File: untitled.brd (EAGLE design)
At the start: 95 x 55 mm, 26 parts, among them IC1 L297, IC2 L298

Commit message: Another commit
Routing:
- net N$9: track 59.8 -> 55.4 mm, vias 0 -> 2
- net N$19: track 80.8 -> 79.5 mm
- net N$8: track 37.3 -> 36.4 mm
- net +24V: track 190.9 -> 190.2 mm, vias 2 -> 0
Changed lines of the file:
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@@
 <wire x1="26" y1="8.035" x2="26" y2="6" width="1.9304" layer="16"/>
 <wire x1="26" y1="6" x2="28" y2="4" width="1.9304" layer="16"/>
-<wire x1="28" y1="4" x2="36" y2="4" width="1.9304" layer="16"/>
-<wire x1="36" y1="4" x2="82" y2="4" width="1.9304" layer="16"/>
+<wire x1="28" y1="4" x2="38" y2="4" width="1.9304" layer="16"/>
+<wire x1="38" y1="4" x2="82" y2="4" width="1.9304" layer="16"/>
 <wire x1="82" y1="4" x2="92" y2="14" width="1.9304" layer="16"/>
 <wire x1="92" y1="14" x2="92" y2="40" width="1.9304" layer="16"/>
@@
 <wire x1="18.73" y1="16.46" x2="18.75" y2="17.98" width="1.9304" layer="16"/>
 <wire x1="65" y1="46.62" x2="65" y2="50.73" width="1.9304" layer="16"/>
-<wire x1="41.54" y1="27.92" x2="38.92" y2="27.92" width="1.778" layer="16"/>
-<wire x1="38.92" y1="27.92" x2="36" y2="25" width="1.778" layer="16"/>
-<wire x1="36" y1="25" x2="36" y2="14" width="1.778" layer="16"/>
-<wire x1="36" y1="4" x2="36" y2="9" width="1.778" layer="16"/>
-<via x="36" y="9" extent="1-16" drill="1" shape="square"/>
-<via x="36" y="14" extent="1-16" drill="1" shape="square"/>
-<wire x1="36" y1="9" x2="36" y2="14" width="0.8128" layer="1"/>
+<wire x1="41.54" y1="27.92" x2="41.54" y2="28" width="1.778" layer="16"/>
+<wire x1="41.54" y1="28" x2="39" y2="28" width="1.778" layer="16"/>
+<wire x1="39" y1="28" x2="38" y2="27" width="1.778" layer="16"/>
+<wire x1="38" y1="27" x2="38" y2="4" width="1.778" layer="16"/>
 </signal>
 <signal name="N$5">
@@
 <wire x1="32.81" y1="31.73" x2="31.73" y2="31.73" width="0.3048" layer="16"/>
 <wire x1="31.73" y1="31.73" x2="30.5" y2="30.5" width="0.3048" layer="16"/>
-<wire x1="30.5" y1="30.5" x2="30.5" y2="16.295" width="0.3048" layer="16"/>
-<wire x1="30.5" y1="16.295" x2="29.07" y2="15.5" width="0.3048" layer="16"/>
+<wire x1="30.5" y1="30.5" x2="30.5" y2="17.295" width="0.3048" layer="16"/>
+<wire x1="30.5" y1="17.295" x2="29.07" y2="15.5" width="0.3048" layer="16"/>
 <wire x1="32.81" y1="31.73" x2="33.27" y2="31.73" width="0.3048" layer="16"/>
 <wire x1="33.27" y1="31.73" x2="34.54" y2="30.46" width="0.3048" layer="16"/>
@@
 <wire x1="25.84" y1="40" x2="27" y2="40" width="0.3048" layer="16"/>
 <wire x1="46.62" y1="41.89" x2="46" y2="42.51" width="0.3048" layer="16"/>
-<wire x1="46" y1="42.51" x2="46" y2="48.5" width="0.3048" layer="16"/>
-<via x="27" y="48.5" extent="1-16" drill="1" shape="square"/>
-<via x="46" y="48.5" extent="1-16" drill="1" shape="square"/>
-<wire x1="27" y1="48.5" x2="46" y2="48.5" width="0.3048" layer="1"/>
-<wire x1="27" y1="48.5" x2="28" y2="47.5" width="0.3048" layer="16"/>
+<wire x1="46" y1="42.51" x2="46" y2="48.25" width="0.3048" layer="16"/>
+<via x="27.25" y="48.25" extent="1-16" drill="1" shape="square"/>
+<via x="46" y="48.25" extent="1-16" drill="1" shape="square"/>
+<wire x1="27.25" y1="48.25" x2="46" y2="48.25" width="0.3048" layer="1"/>
+<wire x1="27.25" y1="48.25" x2="28" y2="47.5" width="0.3048" layer="16"/>
 <wire x1="28" y1="47.5" x2="28" y2="41" width="0.3048" layer="16"/>
 <wire x1="28" y1="41" x2="27" y2="40" width="0.3048" layer="16"/>
@@
 <contactref element="IC1" pad="14"/>
 <contactref element="IC2" pad="1"/>
-<wire x1="25.19" y1="36.81" x2="29" y2="33" width="0.3048" layer="16"/>
-<wire x1="27" y1="13.25" x2="28" y2="12.25" width="0.3048" layer="16"/>
-<wire x1="28" y1="12.25" x2="37" y2="12.25" width="0.3048" layer="16"/>
-<wire x1="37" y1="12.25" x2="38" y2="13.25" width="0.3048" layer="16"/>
-<wire x1="38" y1="13.25" x2="38" y2="25" width="0.3048" layer="16"/>
-<wire x1="38" y1="25" x2="39.75" y2="26.65" width="0.3048" layer="16"/>
-<wire x1="39.75" y1="26.65" x2="43.5" y2="26.65" width="0.3048" layer="16"/>
-<wire x1="43.5" y1="26.65" x2="46.14" y2="24.11" width="0.3048" layer="16"/>
-<wire x1="46.14" y1="24.11" x2="46.62" y2="24.11" width="0.3048" layer="16"/>
-<wire x1="29" y1="33" x2="29" y2="22" width="0.3048" layer="16"/>
-<wire x1="29" y1="22" x2="27" y2="20" width="0.3048" layer="16"/>
-<wire x1="27" y1="20" x2="27" y2="13.25" width="0.3048" layer="16"/>
+<wire x1="25.19" y1="36.81" x2="26.19" y2="36.81" width="0.3048" layer="16"/>
+<wire x1="26.19" y1="36.81" x2="29" y2="34" width="0.3048" layer="16"/>
+<wire x1="29" y1="34" x2="29" y2="21" width="0.3048" layer="16"/>
+<wire x1="29" y1="21" x2="27" y2="19" width="0.3048" layer="16"/>
+<wire x1="27" y1="19" x2="27" y2="14" width="0.3048" layer="16"/>
+<wire x1="27" y1="14" x2="28" y2="13" width="0.3048" layer="16"/>
+<wire x1="28" y1="13" x2="34" y2="13" width="0.3048" layer="16"/>
+<wire x1="34" y1="13" x2="36" y2="15" width="0.3048" layer="16"/>
+<wire x1="36" y1="15" x2="36" y2="22" width="0.3048" layer="16"/>
+<wire x1="46.62" y1="24.11" x2="46.62" y2="22.62" width="0.3048" layer="16"/>
+<wire x1="46.62" y1="22.62" x2="46" y2="22" width="0.3048" layer="16"/>
+<via x="36" y="22" extent="1-16" drill="0.6" shape="square"/>
+<via x="46" y="22" extent="1-16" drill="0.6" shape="square"/>
+<wire x1="36" y1="22" x2="46" y2="22" width="0.3048" layer="1"/>
 </signal>
 <signal name="N$7">
@@
 <wire x1="85" y1="41" x2="72" y2="41" width="1.9304" layer="16"/>
 <wire x1="65" y1="31.38" x2="65" y2="34" width="1.9304" layer="16"/>
-<wire x1="65" y1="34" x2="57" y2="42" width="1.9304" layer="16"/>
-<wire x1="57" y1="42" x2="52" y2="42" width="1.9304" layer="16"/>
-<wire x1="52" y1="42" x2="51" y2="43" width="1.9304" layer="16"/>
-<wire x1="51" y1="43" x2="51" y2="48.25" width="1.9304" layer="16"/>
-<wire x1="51" y1="48.25" x2="49" y2="50.25" width="1.9304" layer="16"/>
-<wire x1="49" y1="50.25" x2="44" y2="50.25" width="1.9304" layer="16"/>
-<wire x1="44" y1="50.25" x2="41.54" y2="47.79" width="1.9304" layer="16"/>
+<wire x1="48.75" y1="51.25" x2="44" y2="51.25" width="1.9304" layer="16"/>
+<wire x1="44" y1="51.25" x2="41.54" y2="47.79" width="1.9304" layer="16"/>
 <wire x1="41.54" y1="47.79" x2="41.54" y2="40.62" width="1.9304" layer="16"/>
 <wire x1="72" y1="41" x2="65" y2="34" width="1.9304" layer="16"/>
+<wire x1="64" y1="34" x2="65" y2="34" width="1.9304" layer="16"/>
+<wire x1="48.75" y1="51.25" x2="64" y2="34" width="1.9304" layer="16"/>
 </signal>
 <signal name="N$20">

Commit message: All traces routed
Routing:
- net N$19: track 79.5 -> 80.6 mm
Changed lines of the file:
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@@
 <wire x1="72" y1="41" x2="65" y2="34" width="1.9304" layer="16"/>
 <wire x1="64" y1="34" x2="65" y2="34" width="1.9304" layer="16"/>
-<wire x1="48.75" y1="51.25" x2="64" y2="34" width="1.9304" layer="16"/>
+<wire x1="48.75" y1="51.25" x2="51" y2="49" width="1.9304" layer="16"/>
+<wire x1="51" y1="49" x2="51" y2="46" width="1.9304" layer="16"/>
+<wire x1="51" y1="46" x2="63" y2="34" width="1.9304" layer="16"/>
+<wire x1="63" y1="34" x2="64" y2="34" width="1.9304" layer="16"/>
 </signal>
 <signal name="N$20">

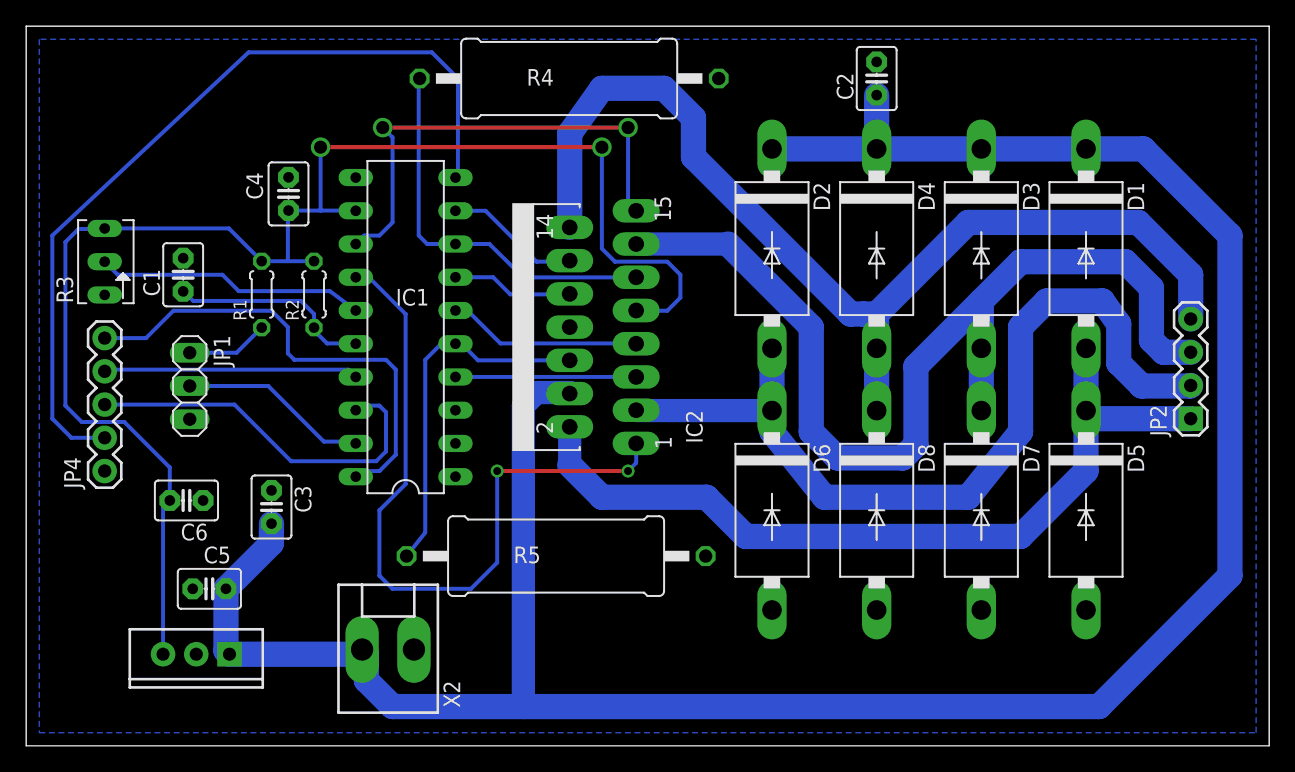
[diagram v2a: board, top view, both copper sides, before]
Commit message: Improved space between traces
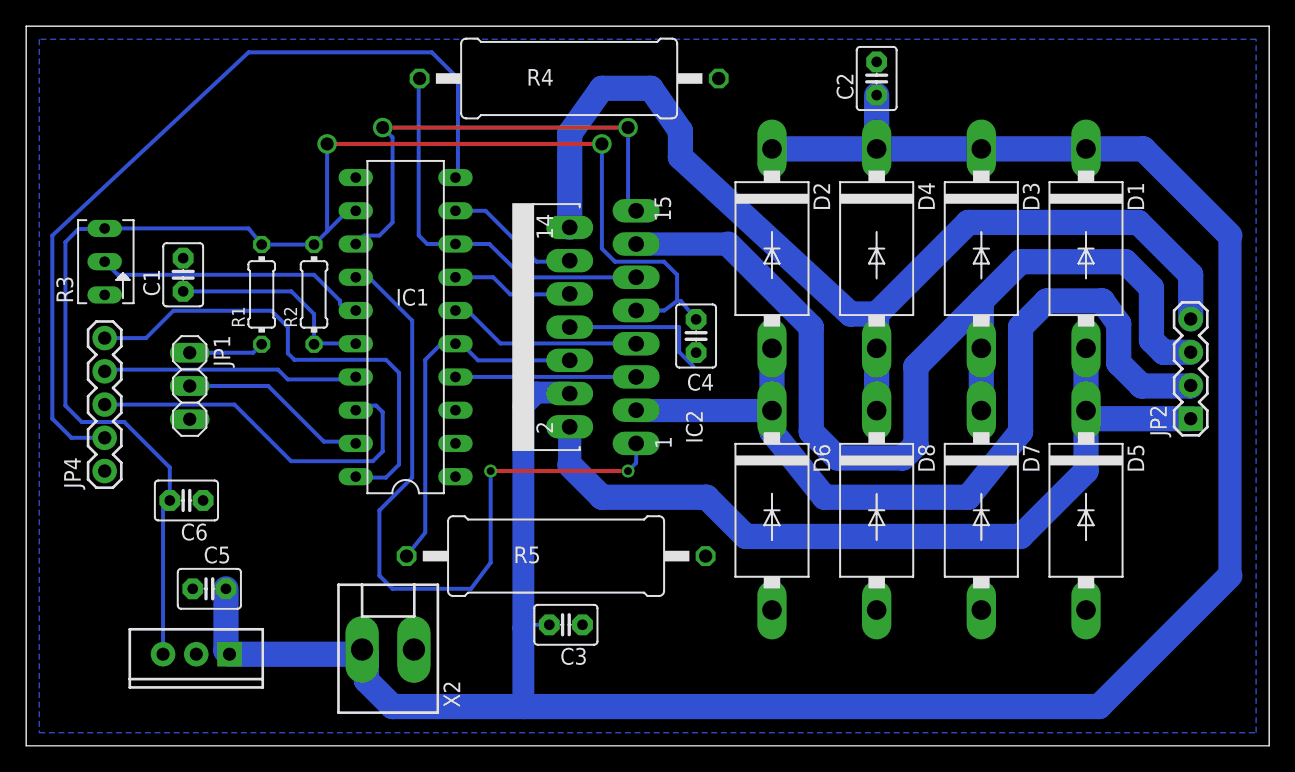
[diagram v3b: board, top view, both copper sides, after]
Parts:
- R1, R2: device resistor:0204/5 -> resistor:0204/7
- moved C4 33.0 mm to (51.2, 32.3), turned to 90 degrees
- moved C3 24.2 mm to (41.2, 10.2), turned to 180 degrees
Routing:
- net GND: track 0.00 -> 11.8 mm
- net +24V: track 190.2 -> 185.8 mm
- net +5V: track 113.7 -> 111.0 mm
- net N$13: track 36.6 -> 37.5 mm
- net N$20: track 15.6 -> 16.2 mm
- net N$9: track 55.4 -> 56.0 mm
- net N$2: track 6.30 -> 5.77 mm
- net N$19: track 80.6 -> 80.1 mm
- net N$11: track 29.3 -> 28.8 mm

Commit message: Se imprime
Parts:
- moved C6 7.91 mm to (7.75, 13.2), turned to 0 degrees
- moved C5 2.75 mm to (16.8, 13.0), turned to 0 degrees
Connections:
- net GND: now also JP4.5; no longer JP4.1
- net N$13: now also JP4.1; no longer JP4.5
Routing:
- net N$13: track 37.5 -> 19.4 mm, vias 0 -> 2
- net +5V: track 111.0 -> 113.3 mm
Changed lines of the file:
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@@
 <attribute name="VALUE" x="33.405" y="3.915" size="1.27" layer="27" rot="R90"/>
 </element>
-<element name="C5" library="capacitor-wima" package="C2.5-3" value="3.3nF" x="14" y="13" smashed="yes" rot="R180">
-<attribute name="NAME" x="15.651" y="16.222" size="1.27" layer="25" ratio="10" rot="R180"/>
-<attribute name="VALUE" x="15.651" y="16.048" size="1.27" layer="27" ratio="10" rot="R180"/>
+<element name="C5" library="capacitor-wima" package="C2.5-3" value="3.3nF" x="16.75" y="13" smashed="yes">
+<attribute name="NAME" x="16.099" y="14.778" size="1.27" layer="25" ratio="10"/>
+<attribute name="VALUE" x="15.099" y="9.952" size="1.27" layer="27" ratio="10"/>
 </element>
-<element name="C6" library="capacitor-wima" package="C2.5-3" value="470uF" x="12.25" y="19.75" rot="R180"/>
+<element name="C6" library="capacitor-wima" package="C2.5-3" value="470uF" x="7.75" y="13.25"/>
 <element name="JP2" library="SparkFun-Connectors" package="1X04" value="" x="89" y="26" rot="R90"/>
 <element name="JP4" library="SparkFun-Connectors" package="1X05" value="" x="6" y="22" rot="R90"/>
@@
 <contactref element="IC3" pad="OUT"/>
 <contactref element="C6" pad="2"/>
-<wire x1="10.46" y1="19.23" x2="10.46" y2="8" width="0.3048" layer="16"/>
 <wire x1="6" y1="40.54" x2="17" y2="40.54" width="0.3048" layer="16"/>
 <wire x1="17" y1="40.54" x2="18" y2="39.31" width="0.3048" layer="16"/>
@@
 <wire x1="5.96" y1="40.5" x2="4" y2="40.5" width="0.3048" layer="16"/>
 <wire x1="4" y1="40.5" x2="3" y2="39.5" width="0.3048" layer="16"/>
-<wire x1="7.5" y1="25.75" x2="10.98" y2="22.27" width="0.3048" layer="16"/>
-<wire x1="10.98" y1="22.27" x2="10.98" y2="19.75" width="0.3048" layer="16"/>
-<wire x1="10.98" y1="19.75" x2="10.46" y2="19.23" width="0.3048" layer="16"/>
+<wire x1="7.5" y1="25.75" x2="11.98" y2="21.27" width="0.3048" layer="16"/>
 <wire x1="18" y1="39.31" x2="22" y2="39.31" width="0.3048" layer="16"/>
 <wire x1="25.19" y1="41.89" x2="24.58" y2="41.89" width="0.3048" layer="16"/>
@@
 <wire x1="49.75" y1="35" x2="50.04" y2="35" width="0.3048" layer="16"/>
 <wire x1="50.04" y1="35" x2="51.2" y2="33.59" width="0.3048" layer="16"/>
+<wire x1="11.98" y1="21.27" x2="12" y2="15" width="0.3048" layer="16"/>
+<wire x1="12" y1="15" x2="10.46" y2="13.46" width="0.3048" layer="16"/>
+<wire x1="10.46" y1="13.46" x2="10.46" y2="8" width="0.3048" layer="16"/>
+<wire x1="10.46" y1="13.46" x2="10.25" y2="13.25" width="0.3048" layer="16"/>
+<wire x1="10.25" y1="13.25" x2="9.02" y2="13.25" width="0.3048" layer="16"/>
 </signal>
 <signal name="GND">
@@
 <vertex x="94" y="55"/>
 </polygon>
-<contactref element="JP4" pad="1"/>
 <wire x1="41.54" y1="33" x2="49.9" y2="33" width="0.3048" layer="16"/>
 <wire x1="49.9" y1="33" x2="49.9" y2="31.1" width="0.3048" layer="16"/>
 <wire x1="49.9" y1="31.1" x2="51" y2="30" width="0.3048" layer="16"/>
+<contactref element="JP4" pad="5"/>
 </signal>
 <signal name="+24V">
@@
 <wire x1="25.675" y1="8.36" x2="25.315" y2="8" width="1.9304" layer="16"/>
 <wire x1="25.315" y1="8" x2="15.54" y2="8" width="1.9304" layer="16"/>
-<wire x1="15.54" y1="8" x2="15.27" y2="8.27" width="1.9304" layer="16"/>
-<wire x1="15.27" y1="8.27" x2="15.27" y2="13" width="1.9304" layer="16"/>
 <wire x1="65" y1="46.62" x2="65" y2="50.73" width="1.9304" layer="16"/>
 <wire x1="41.54" y1="27.92" x2="41.54" y2="28" width="0.3048" layer="16"/>
@@
 <wire x1="39.98" y1="10.25" x2="38.25" y2="10.25" width="0.3048" layer="16"/>
 <wire x1="38.25" y1="10.25" x2="38" y2="10" width="0.3048" layer="16"/>
+<wire x1="15.54" y1="8" x2="15.48" y2="8.06" width="0.3048" layer="16"/>
+<wire x1="15.48" y1="8.06" x2="15.48" y2="13" width="1.016" layer="16"/>
 </signal>
 <signal name="N$5">
@@
 <contactref element="IC2" pad="15"/>
 <contactref element="IC1" pad="13"/>
-<wire x1="25.19" y1="39.35" x2="25.84" y2="40" width="0.3048" layer="16"/>
-<wire x1="25.84" y1="40" x2="27" y2="40" width="0.3048" layer="16"/>
 <wire x1="46.62" y1="41.89" x2="46" y2="42.51" width="0.3048" layer="16"/>
 <wire x1="46" y1="42.51" x2="46" y2="48.25" width="0.3048" layer="16"/>
@@
 <wire x1="27.25" y1="48.25" x2="28" y2="47.5" width="0.3048" layer="16"/>
 <wire x1="28" y1="47.5" x2="28" y2="41" width="0.3048" layer="16"/>
-<wire x1="28" y1="41" x2="27" y2="40" width="0.3048" layer="16"/>
+<wire x1="28" y1="41" x2="26.35" y2="39.35" width="0.3048" layer="16"/>
+<wire x1="26.35" y1="39.35" x2="25.19" y2="39.35" width="0.3048" layer="16"/>
 </signal>
 <signal name="N$9">
@@
 <contactref element="IC2" pad="1"/>
 <wire x1="25.19" y1="36.81" x2="26.19" y2="36.81" width="0.3048" layer="16"/>
-<wire x1="26.19" y1="36.81" x2="29.5" y2="33.5" width="0.3048" layer="16"/>
-<wire x1="29.5" y1="33.5" x2="29.5" y2="21.5" width="0.3048" layer="16"/>
-<wire x1="29.5" y1="21.5" x2="27" y2="19" width="0.3048" layer="16"/>
+<wire x1="26.19" y1="36.81" x2="29.25" y2="33.75" width="0.3048" layer="16"/>
+<wire x1="29.25" y1="33.75" x2="29.25" y2="21.25" width="0.3048" layer="16"/>
+<wire x1="29.25" y1="21.25" x2="27" y2="19" width="0.3048" layer="16"/>
 <wire x1="27" y1="19" x2="27" y2="14" width="0.3048" layer="16"/>
 <wire x1="27" y1="14" x2="28" y2="13" width="0.3048" layer="16"/>
@@
 <wire x1="33" y1="44.62" x2="33" y2="52" width="0.3048" layer="16"/>
 <wire x1="33" y1="52" x2="31" y2="54" width="0.3048" layer="16"/>
+<wire x1="2" y1="40" x2="17" y2="54" width="0.3048" layer="16"/>
+<wire x1="17" y1="54" x2="31" y2="54" width="0.3048" layer="16"/>
 <wire x1="2" y1="40" x2="2" y2="26" width="0.3048" layer="16"/>
 <wire x1="2" y1="26" x2="3.46" y2="24.54" width="0.3048" layer="16"/>
 <wire x1="3.46" y1="24.54" x2="6" y2="24.54" width="0.3048" layer="16"/>
-<wire x1="2" y1="40" x2="17" y2="54" width="0.3048" layer="16"/>
-<wire x1="17" y1="54" x2="31" y2="54" width="0.3048" layer="16"/>
 </signal>
 <signal name="N$11">
 <contactref element="IC1" pad="18"/>
 <contactref element="JP4" pad="3"/>
-<wire x1="26.5" y1="22.75" x2="27.25" y2="23.5" width="0.3048" layer="16"/>
-<wire x1="27.25" y1="23.5" x2="27.25" y2="26.5" width="0.3048" layer="16"/>
-<wire x1="27.25" y1="26.5" x2="26.75" y2="27" width="0.3048" layer="16"/>
-<wire x1="26.75" y1="27" x2="25.54" y2="27" width="0.3048" layer="16"/>
-<wire x1="25.54" y1="27" x2="25.19" y2="26.65" width="0.3048" layer="16"/>
 <wire x1="6" y1="27.08" x2="15.92" y2="27.08" width="0.3048" layer="16"/>
 <wire x1="15.92" y1="27.08" x2="20.25" y2="22.75" width="0.3048" layer="16"/>
-<wire x1="20.25" y1="22.75" x2="26.5" y2="22.75" width="0.3048" layer="16"/>
+<wire x1="20.25" y1="22.75" x2="27" y2="22.75" width="0.3048" layer="16"/>
+<wire x1="27" y1="22.75" x2="28" y2="23.75" width="0.3048" layer="16"/>
+<wire x1="28" y1="23.75" x2="28" y2="25.5" width="0.3048" layer="16"/>
+<wire x1="28" y1="25.5" x2="26.85" y2="26.65" width="0.3048" layer="16"/>
+<wire x1="26.85" y1="26.65" x2="25.19" y2="26.65" width="0.3048" layer="16"/>
 </signal>
 <signal name="N$12">
@@
 <signal name="N$13">
 <contactref element="IC1" pad="20"/>
-<contactref element="JP4" pad="5"/>
-<wire x1="5.84" y1="32" x2="6" y2="32.16" width="0.3048" layer="16"/>
-<wire x1="20.5" y1="30.5" x2="27.5" y2="30.5" width="0.3048" layer="16"/>
-<wire x1="27.5" y1="30.5" x2="28.5" y2="29.5" width="0.3048" layer="16"/>
-<wire x1="28.5" y1="29.5" x2="28.5" y2="22.5" width="0.3048" layer="16"/>
-<wire x1="18.75" y1="34.25" x2="20" y2="33" width="0.3048" layer="16"/>
-<wire x1="20" y1="33" x2="20" y2="31" width="0.3048" layer="16"/>
-<wire x1="20" y1="31" x2="20.5" y2="30.5" width="0.3048" layer="16"/>
-<wire x1="6" y1="32.16" x2="9.16" y2="32.16" width="0.3048" layer="16"/>
-<wire x1="9.16" y1="32.16" x2="11.25" y2="34.25" width="0.3048" layer="16"/>
-<wire x1="11.25" y1="34.25" x2="18.75" y2="34.25" width="0.3048" layer="16"/>
-<wire x1="28.5" y1="22.5" x2="27.5" y2="21.5" width="0.3048" layer="16"/>
-<wire x1="27.5" y1="21.5" x2="25.26" y2="21.5" width="0.3048" layer="16"/>
-<wire x1="25.26" y1="21.5" x2="25.19" y2="21.57" width="0.3048" layer="16"/>
+<contactref element="JP4" pad="1"/>
+<via x="9" y="21.5" extent="1-16" drill="1" shape="square"/>
+<wire x1="9" y1="21.5" x2="17" y2="21.5" width="0.3048" layer="1"/>
+<via x="17" y="21.5" extent="1-16" drill="1" shape="square"/>
+<wire x1="17" y1="21.5" x2="17.07" y2="21.57" width="0.3048" layer="16"/>
+<wire x1="17.07" y1="21.57" x2="25.19" y2="21.57" width="0.3048" layer="16"/>
+<wire x1="9" y1="21.5" x2="8.5" y2="22" width="0.3048" layer="16"/>
+<wire x1="8.5" y1="22" x2="6" y2="22" width="0.3048" layer="16"/>
 </signal>
 <signal name="N$21">

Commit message: Versión 2
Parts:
- removed C6: 470uF, capacitor-wima:C2.5-3
- added C7: 470uF, SparkFun-Capacitors:CPOL-RADIAL-100UF-25V
- C2: device capacitor-wima:C2.5-3 -> SparkFun-Capacitors:CPOL-RADIAL-100UF-25V
- R1, R2: device resistor:0204/7 -> resistor:0207/10
- moved C3 4.74 mm to (36.8, 8.75), turned to 0 degrees
- moved C2 4.00 mm to (61.0, 52.0), turned to 270 degrees
- moved C5 2.00 mm to (16.8, 15.0)
- moved R2 1.35 mm to (21.5, 36.8)
- moved R1 0.50 mm to (18.0, 36.0)
- moved JP2 0.25 mm to (88.8, 26.0)
- moved R4 0.25 mm to (41.2, 52.0)
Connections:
- net +5V: now also C7.1; no longer C6.2
- net GND: now also C7.2; no longer C6.1
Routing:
- net GND: track 11.8 -> 202.6 mm
- net N$10: track 63.6 -> 69.7 mm
- net N$22: track 0.00 -> 5.00 mm
- net +24V: track 185.7 -> 188.7 mm
- net N$9: track 55.8 -> 54.2 mm
- net N$11: track 29.2 -> 28.0 mm
- net +5V: track 113.3 -> 112.7 mm
- added copper zone on layer 16, net +5V
